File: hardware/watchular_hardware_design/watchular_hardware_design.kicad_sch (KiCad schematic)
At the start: 36 parts, among them J1 USB4105-GF-A, J2 665102131822, T1 DMG1013UW-7, U1 MCP73832T-2DCI/OT, U2 ESP32-C3FH4, U3 MIC5524-3.3YMT-TZ, U4 W25Q16JVSSIQ, Y1 40MHz

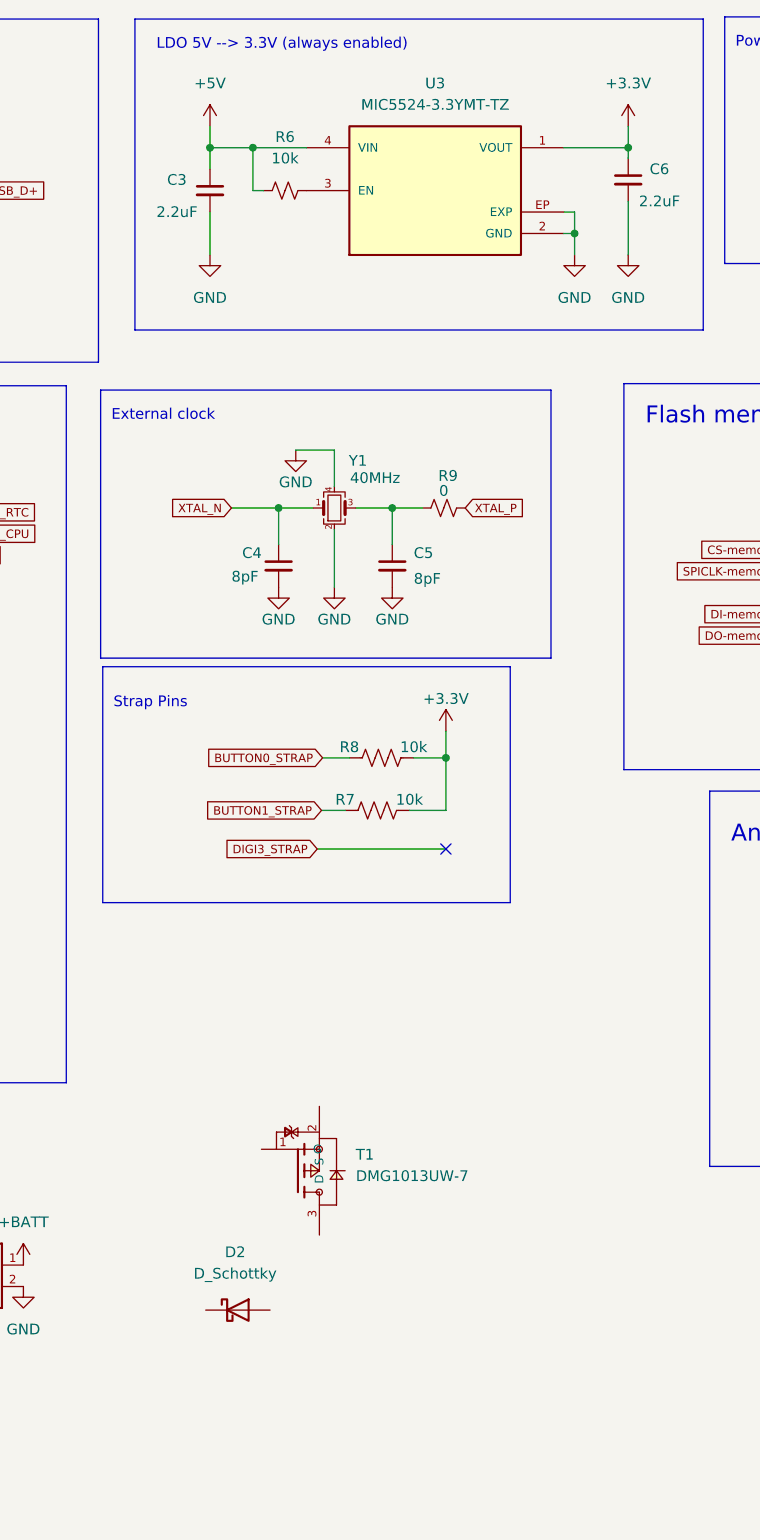
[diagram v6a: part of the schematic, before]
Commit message: Dual power wired up
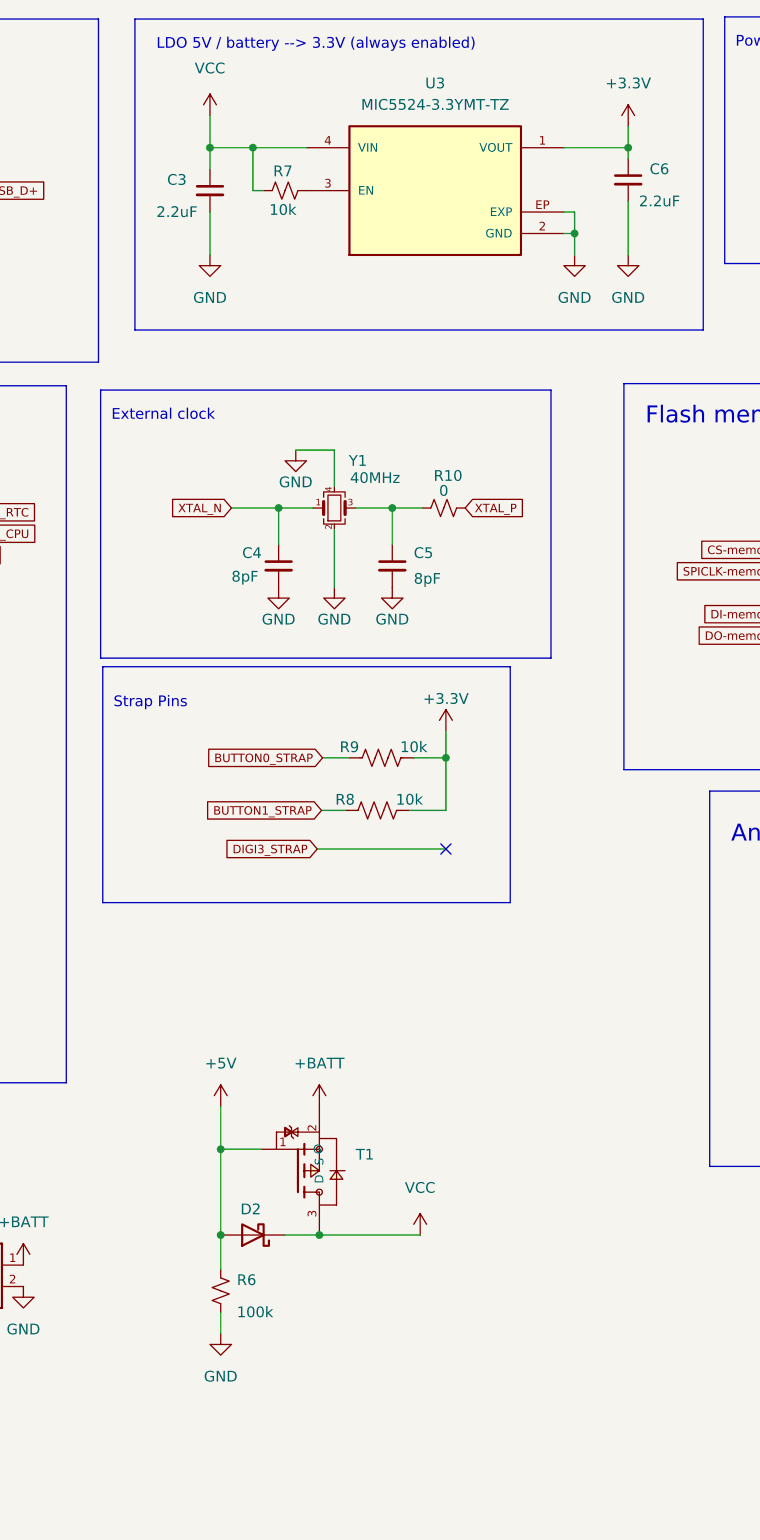
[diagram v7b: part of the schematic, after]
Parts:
- added R6: 100k, Resistor_SMD:R_0402_1005Metric_Pad0.72x0.64mm_HandSolder, symbol Device:R_Small_US
- R10: renamed from R9; footprint Resistor_SMD:R_01005_0402Metric_Pad0.57x0.30mm_HandSolder -> Resistor_SMD:R_0402_1005Metric_Pad0.72x0.64mm_HandSolder
- renumbered R6 to R7, R7 to R8, R8 to R9
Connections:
- net +5V: now also D2.2 (A), T1.1 (G), R6.1; no longer C3.1, R7.1, U3.4 (VIN)
- net +BATT: now also T1.2 (S)
- net GND: now also R6.2
- net VCC: now reaches T1.3 (D)
- net VCC: now also C3.1, D2.1 (K), R7.1, U3.4 (VIN)
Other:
- note added: "LDO 5V / battery --> 3.3V (always enabled)"
- note removed: "LDO 5V --> 3.3V (always enabled)"
- moved on the sheet: D2

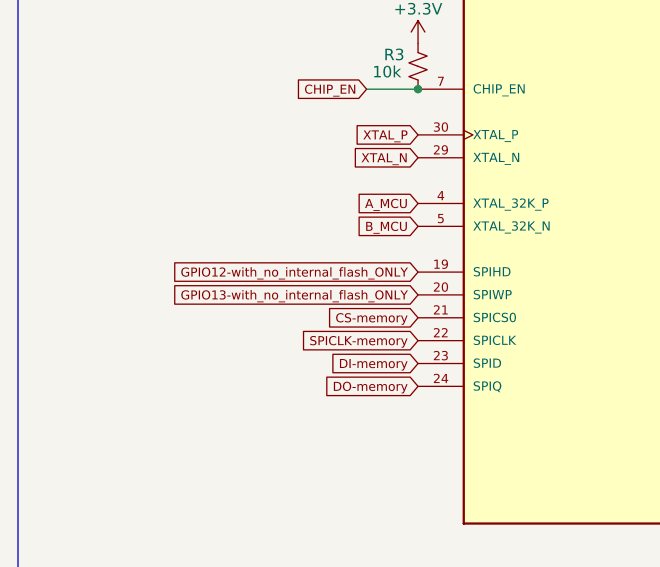
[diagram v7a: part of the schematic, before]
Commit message: Added back the 16 pin headers.
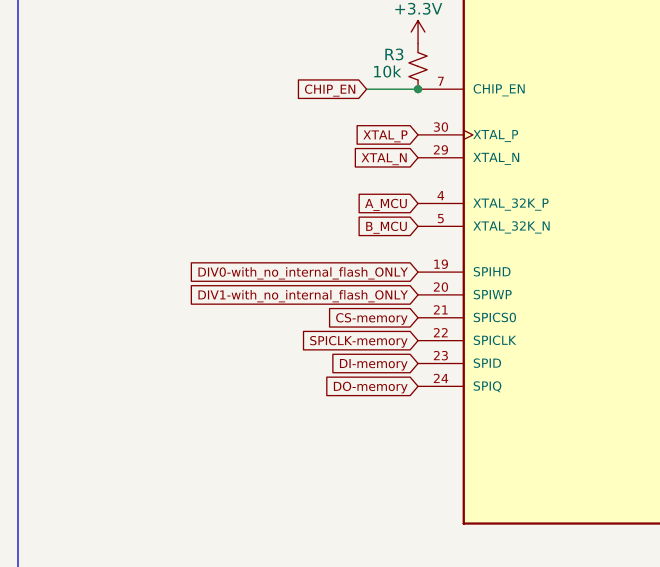
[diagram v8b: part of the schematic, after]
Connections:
- net GPIO12-with_no_internal_flash_ONLY renamed DIV0-with_no_internal_flash_ONLY
- net GPIO13-with_no_internal_flash_ONLY renamed DIV1-with_no_internal_flash_ONLY
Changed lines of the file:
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@@
     )
   )
-  (global_label "GPIO12-with_no_internal_flash_ONLY" (shape input) (at 58.42 105.41 180) (fields_autoplaced)
+  (global_label "DIV0-with_no_internal_flash_ONLY" (shape input) (at 58.42 105.41 180) (fields_autoplaced)
     (effects (font (size 1 1)) (justify right))
-    (property "Intersheet References" "${INTERSHEET_REFS}" (id 0) (at 28.7581 105.3475 0)
+    (property "Intersheet References" "${INTERSHEET_REFS}" (id 0) (at 30.901 105.3475 0)
       (effects (font (size 1 1)) (justify right) hide)
     )
@@
     )
   )
-  (global_label "GPIO13-with_no_internal_flash_ONLY" (shape input) (at 58.42 107.95 180) (fields_autoplaced)
+  (global_label "DIV1-with_no_internal_flash_ONLY" (shape input) (at 58.42 107.95 180) (fields_autoplaced)
     (effects (font (size 1 1)) (justify right))
-    (property "Intersheet References" "${INTERSHEET_REFS}" (id 0) (at 28.7581 107.8875 0)
+    (property "Intersheet References" "${INTERSHEET_REFS}" (id 0) (at 30.901 107.8875 0)
       (effects (font (size 1 1)) (justify right) hide)
     )
@@
       (reference "#PWR045") (unit 1) (value "GND") (footprint "")
     )
+    (path "/4564b4f9-90bf-45c2-8acf-66350b5ba946/7b2e5de1-d3e0-45ec-9f4e-bc3b22297403"
+      (reference "#PWR046") (unit 1) (value "+5V") (footprint "")
+    )
+    (path "/4564b4f9-90bf-45c2-8acf-66350b5ba946/6d48482b-ad23-43ef-8f51-2d9988057054"
+      (reference "#PWR047") (unit 1) (value "GND") (footprint "")
+    )
+    (path "/4564b4f9-90bf-45c2-8acf-66350b5ba946/cfca7857-1c31-435f-9d1f-43785a8068ee"
+      (reference "#PWR048") (unit 1) (value "GND") (footprint "")
+    )
+    (path "/4564b4f9-90bf-45c2-8acf-66350b5ba946/2648135f-e321-43f5-b350-83cd5dfdff7a"
+      (reference "#PWR049") (unit 1) (value "+BATT") (footprint "")
+    )
     (path "/4564b4f9-90bf-45c2-8acf-66350b5ba946/97dd204e-2a06-4a2b-a41c-0bb1913eca42"
-      (reference "#PWR046") (unit 1) (value "GND") (footprint "")
+      (reference "#PWR050") (unit 1) (value "GND") (footprint "")
     )
     (path "/4564b4f9-90bf-45c2-8acf-66350b5ba946/f766da9c-a2d4-4ea2-91de-56ef56d471fe"
-      (reference "#PWR047") (unit 1) (value "GND") (footprint "")
+      (reference "#PWR051") (unit 1) (value "GND") (footprint "")
     )
     (path "/1139fd41-bcfc-4cbe-8f9a-b980537f1914"
@@
       (reference "D16") (unit 1) (value "G") (footprint "LED_SMD:LED_0603_1608Metric")
     )
+    (path "/4564b4f9-90bf-45c2-8acf-66350b5ba946/e1192684-7a60-4158-9b96-cfaa059e45fd"
+      (reference "D17") (unit 1) (value "DVI0") (footprint "LED_SMD:LED_0603_1608Metric")
+    )
+    (path "/4564b4f9-90bf-45c2-8acf-66350b5ba946/45d322f7-111e-4554-aa38-bbb08dafe1b3"
+      (reference "D18") (unit 1) (value "DVI1") (footprint "LED_SMD:LED_0603_1608Metric")
+    )
     (path "/4564b4f9-90bf-45c2-8acf-66350b5ba946/fa9dcf80-f539-425d-9c9a-aabd8a4ef6af"
-      (reference "D17") (unit 1) (value "A") (footprint "LED_SMD:LED_0603_1608Metric")
+      (reference "D19") (unit 1) (value "A") (footprint "LED_SMD:LED_0603_1608Metric")
     )
     (path "/4564b4f9-90bf-45c2-8acf-66350b5ba946/1a895819-2dbf-4329-a013-8f0a10cc3714"
-      (reference "D18") (unit 1) (value "B") (footprint "LED_SMD:LED_0603_1608Metric")
+      (reference "D20") (unit 1) (value "B") (footprint "LED_SMD:LED_0603_1608Metric")
     )
     (path "/4564b4f9-90bf-45c2-8acf-66350b5ba946/56381035-ce96-4463-8aee-603fa0145900"
-      (reference "D19") (unit 1) (value "C") (footprint "LED_SMD:LED_0603_1608Metric")
+      (reference "D21") (unit 1) (value "C") (footprint "LED_SMD:LED_0603_1608Metric")
     )
     (path "/4564b4f9-90bf-45c2-8acf-66350b5ba946/7c21923d-df4a-4594-a2b0-e8195d279336"
-      (reference "D20") (unit 1) (value "D") (footprint "LED_SMD:LED_0603_1608Metric")
+      (reference "D22") (unit 1) (value "D") (footprint "LED_SMD:LED_0603_1608Metric")
     )
     (path "/4564b4f9-90bf-45c2-8acf-66350b5ba946/719e8700-18d8-4758-8f85-fd2c31c57adf"
-      (reference "D21") (unit 1) (value "E") (footprint "LED_SMD:LED_0603_1608Metric")
+      (reference "D23") (unit 1) (value "E") (footprint "LED_SMD:LED_0603_1608Metric")
     )
     (path "/4564b4f9-90bf-45c2-8acf-66350b5ba946/386d9d48-dfc1-4ec5-8f06-a99362691dfc"
-      (reference "D22") (unit 1) (value "F") (footprint "LED_SMD:LED_0603_1608Metric")
+      (reference "D24") (unit 1) (value "F") (footprint "LED_SMD:LED_0603_1608Metric")
     )
     (path "/4564b4f9-90bf-45c2-8acf-66350b5ba946/16c98362-9e66-4f73-b236-379ecafe94bf"
-      (reference "D23") (unit 1) (value "G") (footprint "LED_SMD:LED_0603_1608Metric")
+      (reference "D25") (unit 1) (value "G") (footprint "LED_SMD:LED_0603_1608Metric")
     )
     (path "/4564b4f9-90bf-45c2-8acf-66350b5ba946/29edcc67-8c63-4123-8d2e-36c0b5fd62d0"
-      (reference "D24") (unit 1) (value "A") (footprint "LED_SMD:LED_0603_1608Metric")
+      (reference "D26") (unit 1) (value "A") (footprint "LED_SMD:LED_0603_1608Metric")
     )
     (path "/4564b4f9-90bf-45c2-8acf-66350b5ba946/60d50255-f7ab-44c1-87ca-f6a993820e01"
-      (reference "D25") (unit 1) (value "B") (footprint "LED_SMD:LED_0603_1608Metric")
+      (reference "D27") (unit 1) (value "B") (footprint "LED_SMD:LED_0603_1608Metric")
     )
     (path "/4564b4f9-90bf-45c2-8acf-66350b5ba946/c4365d56-1da6-4f5f-af54-08278d1fffdb"
-      (reference "D26") (unit 1) (value "C") (footprint "LED_SMD:LED_0603_1608Metric")
+      (reference "D28") (unit 1) (value "C") (footprint "LED_SMD:LED_0603_1608Metric")
     )
     (path "/4564b4f9-90bf-45c2-8acf-66350b5ba946/1df903f7-0506-4017-9235-f26cd5871406"
-      (reference "D27") (unit 1) (value "D") (footprint "LED_SMD:LED_0603_1608Metric")
+      (reference "D29") (unit 1) (value "D") (footprint "LED_SMD:LED_0603_1608Metric")
     )
     (path "/4564b4f9-90bf-45c2-8acf-66350b5ba946/dccc4e1d-89f0-4ddc-b4cd-1824ae192fba"
-      (reference "D28") (unit 1) (value "E") (footprint "LED_SMD:LED_0603_1608Metric")
+      (reference "D30") (unit 1) (value "E") (footprint "LED_SMD:LED_0603_1608Metric")
     )
     (path "/4564b4f9-90bf-45c2-8acf-66350b5ba946/abaed0df-abb5-45a1-9176-345b1a98de1f"
-      (reference "D29") (unit 1) (value "F") (footprint "LED_SMD:LED_0603_1608Metric")
+      (reference "D31") (unit 1) (value "F") (footprint "LED_SMD:LED_0603_1608Metric")
     )
     (path "/4564b4f9-90bf-45c2-8acf-66350b5ba946/a313074b-f28b-4d5c-87b2-95b135490d04"
-      (reference "D30") (unit 1) (value "G") (footprint "LED_SMD:LED_0603_1608Metric")
+      (reference "D32") (unit 1) (value "G") (footprint "LED_SMD:LED_0603_1608Metric")
     )
     (path "/5f564226-45db-47b5-8947-3a6e6bb5b8e6"
@@
       (reference "J2") (unit 1) (value "665102131822") (footprint "battery_connector-665102131822:665102131822")
     )
-    (path "/4564b4f9-90bf-45c2-8acf-66350b5ba946/d28e1308-70e7-4ba2-8e9f-b0f2255fae00"
-      (reference "J3") (unit 1) (value "TSW-115-07-H-S") (footprint "header-TSW-115-07-H-S:SAMTEC_TSW-115-07-H-S")
-    )
-    (path "/4564b4f9-90bf-45c2-8acf-66350b5ba946/c743158b-46ad-42f9-b58f-5342cfaffe38"
-      (reference "J4") (unit 1) (value "TSW-115-07-H-S") (footprint "header-TSW-115-07-H-S:SAMTEC_TSW-115-07-H-S")
+    (path "/4564b4f9-90bf-45c2-8acf-66350b5ba946/826f6b0d-2967-455b-b765-bd5ed3c19940"
+      (reference "J3") (unit 1) (value "TSW-116-07-H-S") (footprint "SAMTEC_TSW-116-07-H-S")
+    )
+    (path "/4564b4f9-90bf-45c2-8acf-66350b5ba946/e15366f3-44b0-4b8c-b6a5-2e85ec5d7c4c"
+      (reference "J4") (unit 1) (value "TSW-116-07-H-S") (footprint "SAMTEC_TSW-116-07-H-S")
     )
     (path "/1f1de665-878b-408f-bbe7-a6c746e0bfb6"
@@
       (reference "R19") (unit 1) (value "1k") (footprint "Resistor_SMD:R_0402_1005Metric_Pad0.72x0.64mm_HandSolder")
     )
+    (path "/4564b4f9-90bf-45c2-8acf-66350b5ba946/3225c00e-973e-46d4-9a59-b91c1275b453"
+      (reference "R20") (unit 1) (value "560") (footprint "Resistor_SMD:R_0402_1005Metric_Pad0.72x0.64mm_HandSolder")
+    )
+    (path "/4564b4f9-90bf-45c2-8acf-66350b5ba946/183f4c8b-fbe1-4649-b2c7-e19e0a4482a0"
+      (reference "R21") (unit 1) (value "560") (footprint "Resistor_SMD:R_0402_1005Metric_Pad0.72x0.64mm_HandSolder")
+    )
     (path "/4564b4f9-90bf-45c2-8acf-66350b5ba946/1893874f-222a-445a-bd1d-b1d84167c241"
-      (reference "R20") (unit 1) (value "1k") (footprint "Resistor_SMD:R_0402_1005Metric_Pad0.72x0.64mm_HandSolder")
+      (reference "R22") (unit 1) (value "1k") (footprint "Resistor_SMD:R_0402_1005Metric_Pad0.72x0.64mm_HandSolder")
     )
     (path "/4564b4f9-90bf-45c2-8acf-66350b5ba946/4b0f32d1-e6cf-4e1a-98e7-7e0e9ba290c0"
-      (reference "R21") (unit 1) (value "1k") (footprint "Resistor_SMD:R_0402_1005Metric_Pad0.72x0.64mm_HandSolder")
+      (reference "R23") (unit 1) (value "1k") (footprint "Resistor_SMD:R_0402_1005Metric_Pad0.72x0.64mm_HandSolder")
     )
     (path "/4564b4f9-90bf-45c2-8acf-66350b5ba946/f83ace1e-67f8-4df7-80b0-06ff1f4916d0"
